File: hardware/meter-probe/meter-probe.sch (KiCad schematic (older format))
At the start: 0 parts

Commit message: Added some sheets and more components to the main board schematics
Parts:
- added C? (x2): 1uF, symbol Device:C
- added C?: 22nF, symbol Device:C
- added C?: 0.1uF, symbol Device:C
- added J?: Conn_01x05, symbol Connector_Generic:Conn_01x05
- added SW?: SW_Key_6425_0101, lib_fp:SW_Key_6425_0101, symbol Marquadt_Switch:SW_Key_6425_0101
- added U?: RT9193, Package_TO_SOT_SMD:SOT-23-5, symbol Project:RT9193
- added U?: TCS3472, lib_fp:AMS_TCS3472_DFN-6, symbol Project:TCS3472
- added U?: P82B96, Package_SO:SOIC-8_3.9x4.9mm_P1.27mm, symbol Interface_Expansion:P82B96
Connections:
- new net: C?.1, U?.4 (BP)
- new net: U?.2 (RXD-SDA), U?.3 (TXD-SDA)
- new net: U?.5 (TXD-SCL), U?.6 (RXD-SCL)
- new net +3V3: C?.1, C?.2, U?.1 (VDD), U?.5 (VOUT)
- new net +5V: C?.1, U?.1 (VIN), U?.3 (EN), U?.8 (VCC)
- new net GND: C?.1, C?.2, C?.2, C?.2, U?.2 (GND), U?.3 (GND), U?.4 (GND)

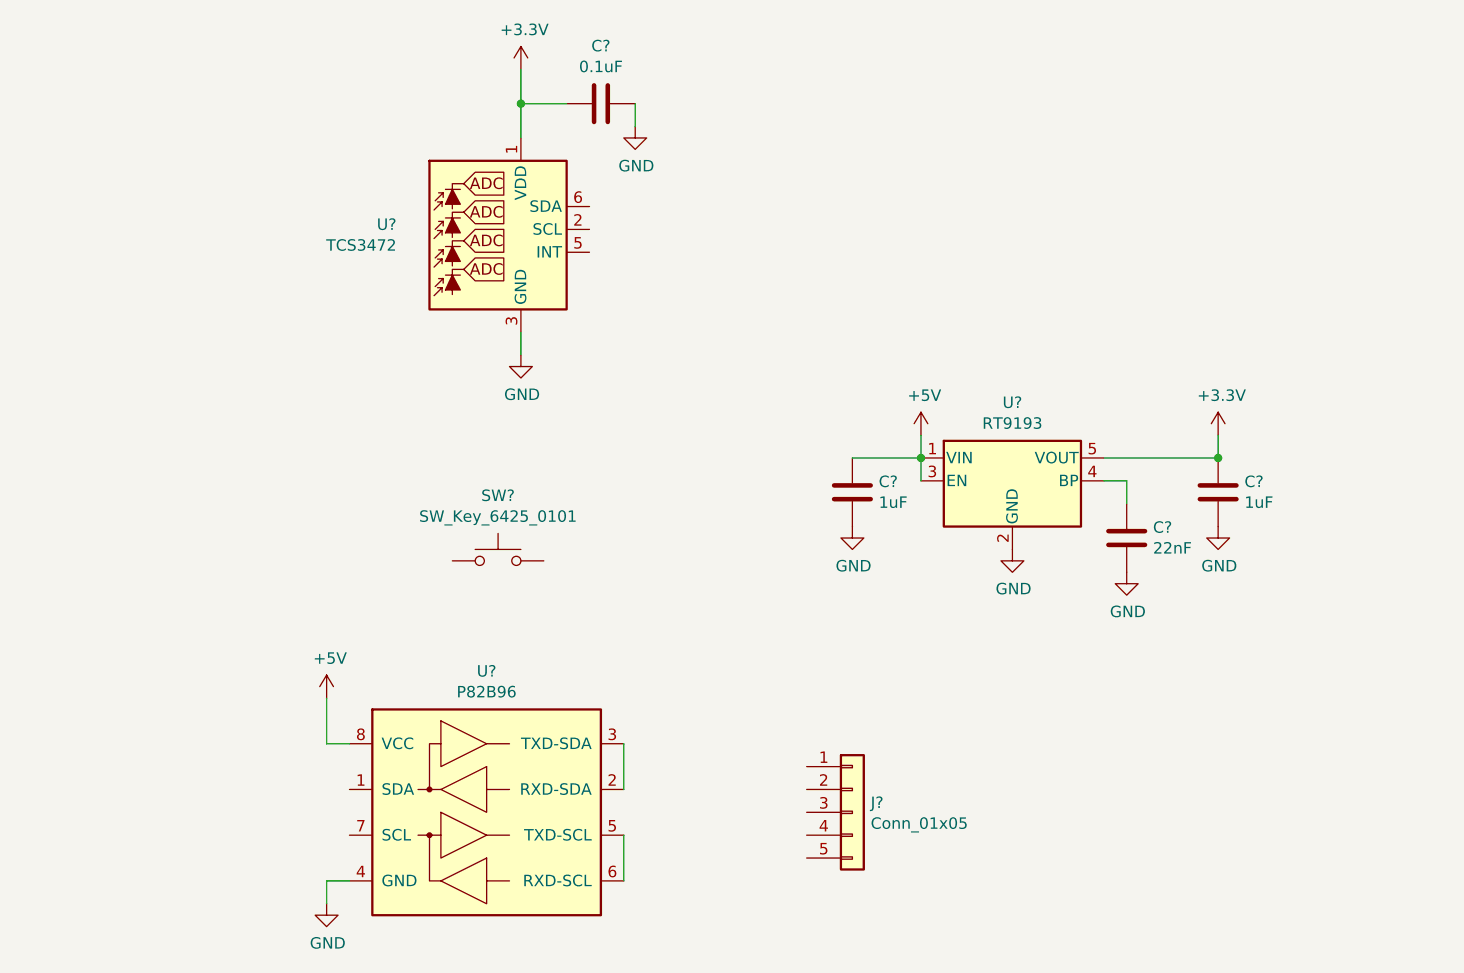
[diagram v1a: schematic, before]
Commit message: Added some off-board I2C interface elements
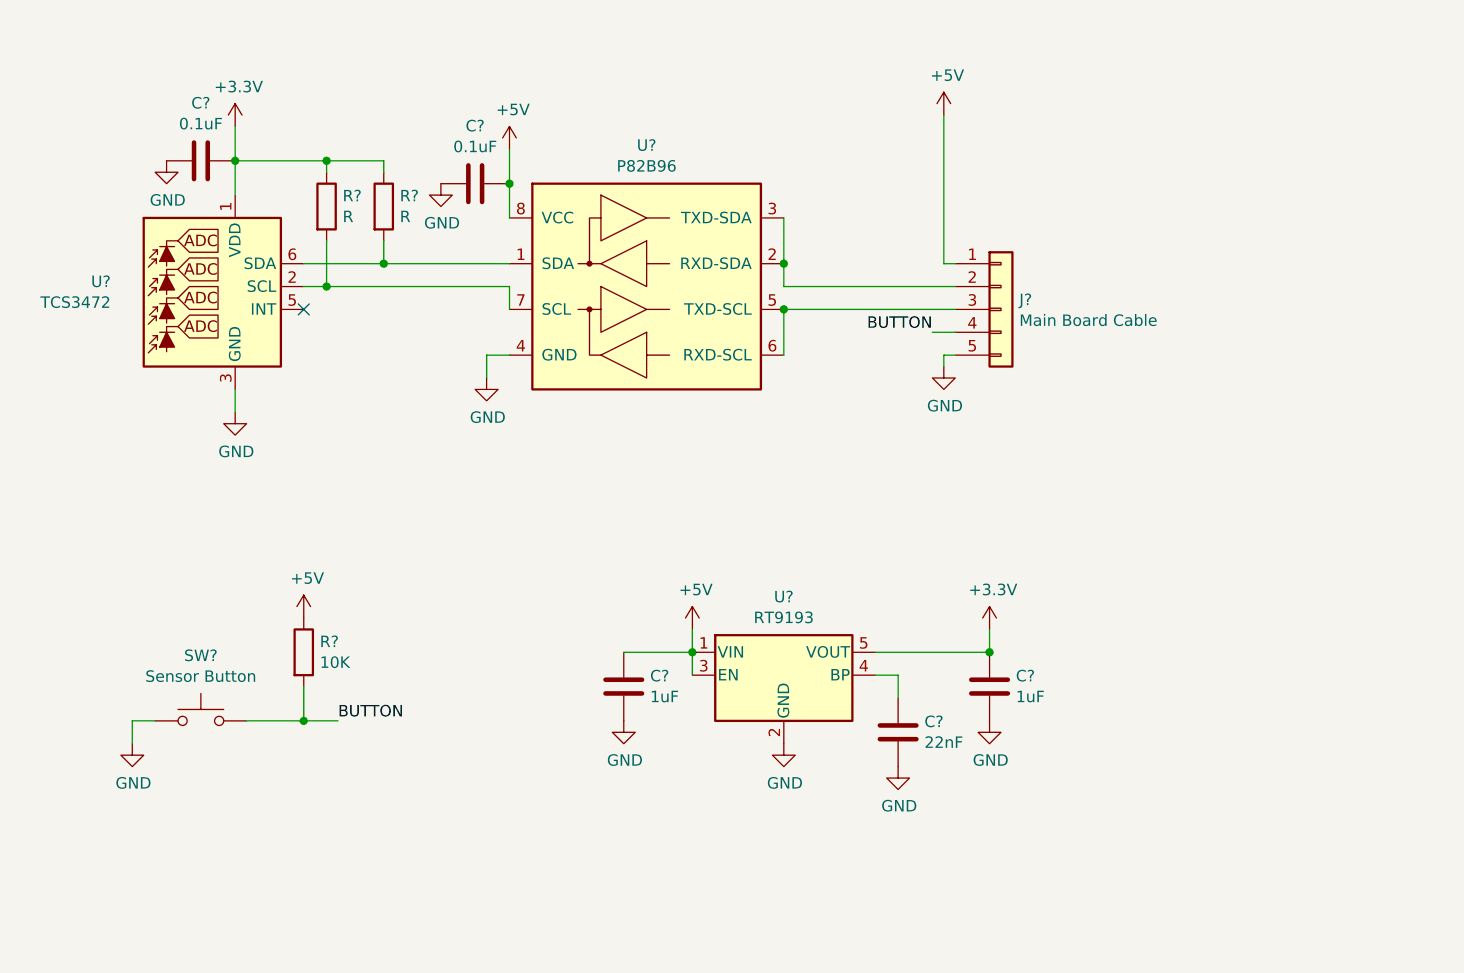
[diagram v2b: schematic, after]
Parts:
- added C?: 0.1uF, symbol Device:C
- added R? (x2): R, symbol Device:R
- added R?: 10K, symbol Device:R
- J?: value Conn_01x05 -> Main Board Cable
- SW?: value SW_Key_6425_0101 -> Sensor Button
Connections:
- net +3V3: now also C?.1, R?.1, R?.1; no longer C?.2
- net +5V: now also J?.1 (Pin_1), C?.1, R?.1
- net GND: now also C?.2, J?.5 (Pin_5), SW?.1, C?.2; no longer C?.1
- net at U?.2 (SCL): now also U?.7 (SCL), R?.2
- net at U?.6 (SDA): now also U?.1 (SDA), R?.2
- net BUTTON: now reaches SW?.2
- net BUTTON: now also J?.4 (Pin_4), R?.2
- net at U?.2 (RXD-SDA), U?.3 (TXD-SDA): now also J?.2 (Pin_2)
- net at U?.5 (TXD-SCL), U?.6 (RXD-SCL): now also J?.3 (Pin_3)
- no-connect marks 0 -> 1
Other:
- moved on the sheet: C?, J?, SW?, U?

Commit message: Sensor probe schematic and BOM associations complete
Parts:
- removed C? (x2): 1uF, symbol Device:C
- removed C?: 22nF, symbol Device:C
- removed C? (x2): 0.1uF, symbol Device:C
- removed R? (x2): R, symbol Device:R
- removed R?: 10K, symbol Device:R
- added C1, C2: 1uF, Capacitor_SMD:C_0805_2012Metric, symbol Device:C_Small
- added C3: 22nF, Capacitor_SMD:C_0805_2012Metric, symbol Device:C_Small
- added C4, C5: 0.1uF, Capacitor_SMD:C_0805_2012Metric, symbol Device:C_Small
- added Q1: BSS138, Package_TO_SOT_SMD:SOT-23, symbol Transistor_FET:BSS138
- added R1, R4, R5: 10K, Resistor_SMD:R_0805_2012Metric, symbol Device:R_Small
- added R2, R3: 2K, Resistor_SMD:R_0805_2012Metric, symbol Device:R_Small
- J1: renamed from J?; value Main Board Cable -> Main Board; footprint (none) -> Connector_Wire:SolderWire-1sqmm_1x06_P5.4mm_D1.4mm_OD2.7mm; symbol Connector_Generic:Conn_01x05 -> Connector_Generic:Conn_01x06
- SW1: renamed from SW?; Description (none) -> Switch 6425.0101 with button 827.100.011; Manufacturer (none) -> Marquardt Switches; Manufacturer PN (none) -> 6425.0101; Supplier (none) -> Mouser; Supplier PN (none) -> 979-6425.0101
- U1: renamed from U?; Description (none) -> IC REG LINEAR 3.3V 300MA SOT23-5; Manufacturer (none) -> Richtek USA Inc.; Manufacturer PN (none) -> RT9193-33GB; Supplier (none) -> Digi-Key; Supplier PN (none) -> 1028-1014-1-ND
- U2: renamed from U?; Description (none) -> IC COLOR CONV LIGHT-DGTL 6-DFN; Manufacturer (none) -> ams; Manufacturer PN (none) -> TCS34725FN; Supplier (none) -> Digi-Key; Supplier PN (none) -> TCS34725FNCT-ND
- U3: renamed from U?; Description (none) -> IC REDRIVER I2C 1CH 400KHZ 8SOIC; Manufacturer (none) -> Texas Instruments; Manufacturer PN (none) -> P82B96DR; Supplier (none) -> Digi-Key; Supplier PN (none) -> 296-20942-1-ND
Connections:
- net +3V3: now also C2.2, C4.1, Q1.1 (G), R2.1, R3.1, R4.1
- net +5V: now also J1.4 (Pin_4), C1.2, C5.1, R1.1, R5.1; no longer J1.1 (Pin_1)
- net GND: now also J1.3 (Pin_3), C1.1, C2.1, C3.1, C4.2, C5.2; no longer J1.5 (Pin_5)
- net at U1.4 (BP): now also C3.2
- net at U2.2 (SCL), U3.7 (SCL): now also R2.2
- net at U2.5 (INT): now also Q1.2 (S), R4.2
- net at U2.6 (SDA), U3.1 (SDA): now also R3.2
- net SDA: now reaches U3.2 (RXD-SDA), U3.3 (TXD-SDA)
- net SDA: now also J1.1 (Pin_1); no longer J1.2 (Pin_2)
- net SCL: now reaches U3.5 (TXD-SCL), U3.6 (RXD-SCL)
- net SCL: now also J1.5 (Pin_5); no longer J1.3 (Pin_3)
- net BUTTON renamed ~BUTTON
- net ~BUTTON: now also J1.6 (Pin_6), R1.2; no longer J1.4 (Pin_4)
- new net ~INT: J1.2 (Pin_2), Q1.3 (D), R5.2
- no-connect marks 1 -> 0
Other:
- note added: "Color light sensor"
- note added: "Level shifting"
- note added: "Main board cable connection"
- note added: "Note: All signals on the cable are at 5V,\nand are level-shifted on this board\nas necessary."
- note added: "Trigger button"
- note added: "Voltage regulator"
- moved on the sheet: SW1, U1, U3

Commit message: Updated wire connection footprint and PCB labeling
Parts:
- J1: footprint Connector_Wire:SolderWire-1sqmm_1x06_P5.4mm_D1.4mm_OD2.7mm -> Connector_Wire:SolderWire-0.1sqmm_1x06_P3.6mm_D0.4mm_OD1mm
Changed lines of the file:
@@
 F 0 "J1" H 5950 1850 50  0000 L CNN
 F 1 "Main Board" H 5900 1150 50  0000 L CNN
-F 2 "Connector_Wire:SolderWire-1sqmm_1x06_P5.4mm_D1.4mm_OD2.7mm" H 6000 1550 50  0001 C CNN
+F 2 "Connector_Wire:SolderWire-0.1sqmm_1x06_P3.6mm_D0.4mm_OD1mm" H 6000 1550 50  0001 C CNN
 F 3 "~" H 6000 1550 50  0001 C CNN
 	1    6000 1550

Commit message: Changed wire-to-board footprint for the meter probe
Created a footprint with more compact pin spacing, that includes
mechanical holes for attaching a cable tie that acts as a strain
relief for the cable.

Increased the length of the board, still within the package space,
to accommodate this change.
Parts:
- J1: footprint Connector_Wire:SolderWire-0.1sqmm_1x06_P3.6mm_D0.4mm_OD1mm -> lib_fp:SolderWire-0.1sqmm_1x06_Cable
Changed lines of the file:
@@
 F 0 "J1" H 5950 1850 50  0000 L CNN
 F 1 "Main Board" H 5900 1150 50  0000 L CNN
-F 2 "Connector_Wire:SolderWire-0.1sqmm_1x06_P3.6mm_D0.4mm_OD1mm" H 6000 1550 50  0001 C CNN
+F 2 "lib_fp:SolderWire-0.1sqmm_1x06_Cable" H 6000 1550 50  0001 C CNN
 F 3 "~" H 6000 1550 50  0001 C CNN
 	1    6000 1550

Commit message: Changed from 0805 to 0602 for passives, and fixed 22nF part
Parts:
- C1, C2: footprint Capacitor_SMD:C_0805_2012Metric -> Capacitor_SMD:C_0603_1608Metric; Description CAP CER 1UF 25V X7R 0805 -> CAP CER 1UF 25V X7R 0603; Manufacturer PN CL21B105KAFNNNE -> CL10B105KA8NNNC; Supplier PN 1276-1066-1-ND -> 1276-1184-1-ND
- C3: Description CAP CER 22PF 50V C0G/NP0 0805 -> CAP CER 0.022UF 50V C0G 0805; Manufacturer Samsung Electro-Mechanics -> TDK Corporation; Manufacturer PN CL21C220JBANNNC -> C2012C0G1H223J125AA; Supplier PN 1276-1047-1-ND -> 445-7522-1-ND
- C4, C5: footprint Capacitor_SMD:C_0805_2012Metric -> Capacitor_SMD:C_0603_1608Metric; Description CAP CER 0.1UF 25V X7R 0805 -> CAP CER 0.1UF 25V X7R 0603; Manufacturer PN CL21B104KACNNNC -> CL10B104KA8NNNC; Supplier PN 1276-1099-1-ND -> 1276-1006-1-ND
- J1: Description (none) -> WIRE-TO-BOARD
- R1, R4, R5: footprint Resistor_SMD:R_0805_2012Metric -> Resistor_SMD:R_0603_1608Metric; Description RES SMD 10K OHM 5% 1/8W 0805 -> RES SMD 10K OHM 5% 1/10W 0603; Manufacturer PN CRCW080510K0JNEA -> CRCW060310K0JNEA; Supplier PN 541-10KACT-ND -> 541-10KGCT-ND
- R2, R3: footprint Resistor_SMD:R_0805_2012Metric -> Resistor_SMD:R_0603_1608Metric; Description RES SMD 2K OHM 5% 1/8W 0805 -> RES SMD 2K OHM 5% 1/10W 0603; Manufacturer PN CRCW08052K00JNEA -> CRCW06032K00JNEA; Supplier PN 541-2.0KACT-ND -> 541-2.0KGCT-ND
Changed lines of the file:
@@
 F 2 "lib_fp:SolderWire-0.1sqmm_1x06_Cable" H 6000 1550 50  0001 C CNN
 F 3 "~" H 6000 1550 50  0001 C CNN
+F 4 "WIRE-TO-BOARD" H 6000 1550 50  0001 C CNN "Description"
 	1    6000 1550
 	1    0    0    -1
@@
 F 0 "R4" H 3559 2946 50  0000 L CNN
 F 1 "10K" H 3559 2855 50  0000 L CNN
-F 2 "Resistor_SMD:R_0805_2012Metric" H 3500 2900 50  0001 C CNN
+F 2 "Resistor_SMD:R_0603_1608Metric" H 3500 2900 50  0001 C CNN
 F 3 "https://www.vishay.com/docs/20035/dcrcwe3.pdf" H 3500 2900 50  0001 C CNN
-F 4 "RES SMD 10K OHM 5% 1/8W 0805" H 3500 2900 50  0001 C CNN "Description"
+F 4 "RES SMD 10K OHM 5% 1/10W 0603" H 3500 2900 50  0001 C CNN "Description"
 F 5 "Vishay Dale" H 3500 2900 50  0001 C CNN "Manufacturer"
-F 6 "CRCW080510K0JNEA" H 3500 2900 50  0001 C CNN "Manufacturer PN"
+F 6 "CRCW060310K0JNEA" H 3500 2900 50  0001 C CNN "Manufacturer PN"
 F 7 "Digi-Key" H 3500 2900 50  0001 C CNN "Supplier"
-F 8 "541-10KACT-ND" H 3500 2900 50  0001 C CNN "Supplier PN"
+F 8 "541-10KGCT-ND" H 3500 2900 50  0001 C CNN "Supplier PN"
 	1    3500 2900
 	1    0    0    -1
@@
 F 0 "R5" H 4259 2946 50  0000 L CNN
 F 1 "10K" H 4259 2855 50  0000 L CNN
-F 2 "Resistor_SMD:R_0805_2012Metric" H 4200 2900 50  0001 C CNN
+F 2 "Resistor_SMD:R_0603_1608Metric" H 4200 2900 50  0001 C CNN
 F 3 "https://www.vishay.com/docs/20035/dcrcwe3.pdf" H 4200 2900 50  0001 C CNN
-F 4 "RES SMD 10K OHM 5% 1/8W 0805" H 4200 2900 50  0001 C CNN "Description"
+F 4 "RES SMD 10K OHM 5% 1/10W 0603" H 4200 2900 50  0001 C CNN "Description"
 F 5 "Vishay Dale" H 4200 2900 50  0001 C CNN "Manufacturer"
-F 6 "CRCW080510K0JNEA" H 4200 2900 50  0001 C CNN "Manufacturer PN"
+F 6 "CRCW060310K0JNEA" H 4200 2900 50  0001 C CNN "Manufacturer PN"
 F 7 "Digi-Key" H 4200 2900 50  0001 C CNN "Supplier"
-F 8 "541-10KACT-ND" H 4200 2900 50  0001 C CNN "Supplier PN"
+F 8 "541-10KGCT-ND" H 4200 2900 50  0001 C CNN "Supplier PN"
 	1    4200 2900
 	1    0    0    -1
@@
 F 0 "R2" H 2259 1646 50  0000 L CNN
 F 1 "2K" H 2259 1555 50  0000 L CNN
-F 2 "Resistor_SMD:R_0805_2012Metric" H 2200 1600 50  0001 C CNN
+F 2 "Resistor_SMD:R_0603_1608Metric" H 2200 1600 50  0001 C CNN
 F 3 "https://www.vishay.com/docs/20035/dcrcwe3.pdf" H 2200 1600 50  0001 C CNN
-F 4 "RES SMD 2K OHM 5% 1/8W 0805" H 2200 1600 50  0001 C CNN "Description"
+F 4 "RES SMD 2K OHM 5% 1/10W 0603" H 2200 1600 50  0001 C CNN "Description"
 F 5 "Vishay Dale" H 2200 1600 50  0001 C CNN "Manufacturer"
-F 6 "CRCW08052K00JNEA" H 2200 1600 50  0001 C CNN "Manufacturer PN"
+F 6 "CRCW06032K00JNEA" H 2200 1600 50  0001 C CNN "Manufacturer PN"
 F 7 "Digi-Key" H 2200 1600 50  0001 C CNN "Supplier"
-F 8 "541-2.0KACT-ND" H 2200 1600 50  0001 C CNN "Supplier PN"
+F 8 "541-2.0KGCT-ND" H 2200 1600 50  0001 C CNN "Supplier PN"
 	1    2200 1600
 	1    0    0    -1
@@
 F 0 "R3" H 2509 1646 50  0000 L CNN
 F 1 "2K" H 2509 1555 50  0000 L CNN
-F 2 "Resistor_SMD:R_0805_2012Metric" H 2450 1600 50  0001 C CNN
+F 2 "Resistor_SMD:R_0603_1608Metric" H 2450 1600 50  0001 C CNN
 F 3 "https://www.vishay.com/docs/20035/dcrcwe3.pdf" H 2450 1600 50  0001 C CNN
-F 4 "RES SMD 2K OHM 5% 1/8W 0805" H 2450 1600 50  0001 C CNN "Description"
+F 4 "RES SMD 2K OHM 5% 1/10W 0603" H 2450 1600 50  0001 C CNN "Description"
 F 5 "Vishay Dale" H 2450 1600 50  0001 C CNN "Manufacturer"
-F 6 "CRCW08052K00JNEA" H 2450 1600 50  0001 C CNN "Manufacturer PN"
+F 6 "CRCW06032K00JNEA" H 2450 1600 50  0001 C CNN "Manufacturer PN"
 F 7 "Digi-Key" H 2450 1600 50  0001 C CNN "Supplier"
-F 8 "541-2.0KACT-ND" H 2450 1600 50  0001 C CNN "Supplier PN"
+F 8 "541-2.0KGCT-ND" H 2450 1600 50  0001 C CNN "Supplier PN"
 	1    2450 1600
 	1    0    0    -1
@@
 F 0 "C4" V 1371 1400 50  0000 C CNN
 F 1 "0.1uF" V 1462 1400 50  0000 C CNN
-F 2 "Capacitor_SMD:C_0805_2012Metric" H 1600 1400 50  0001 C CNN
-F 3 "https://media.digikey.com/pdf/Data%20Sheets/Samsung%20PDFs/CL21B104KACNNNC_Spec.pdf" H 1600 1400 50  0001 C CNN
-F 4 "CAP CER 0.1UF 25V X7R 0805" H 1600 1400 50  0001 C CNN "Description"
+F 2 "Capacitor_SMD:C_0603_1608Metric" H 1600 1400 50  0001 C CNN
+F 3 "https://media.digikey.com/pdf/Data%20Sheets/Samsung%20PDFs/CL_Series_MLCC_ds.pdf" H 1600 1400 50  0001 C CNN
+F 4 "CAP CER 0.1UF 25V X7R 0603" H 1600 1400 50  0001 C CNN "Description"
 F 5 "Samsung Electro-Mechanics" H 1600 1400 50  0001 C CNN "Manufacturer"
-F 6 "CL21B104KACNNNC" H 1600 1400 50  0001 C CNN "Manufacturer PN"
+F 6 "CL10B104KA8NNNC" H 1600 1400 50  0001 C CNN "Manufacturer PN"
 F 7 "Digi-Key" H 1600 1400 50  0001 C CNN "Supplier"
-F 8 "1276-1099-1-ND" H 1600 1400 50  0001 C CNN "Supplier PN"
+F 8 "1276-1006-1-ND" H 1600 1400 50  0001 C CNN "Supplier PN"
 	1    1600 1400
 	0    1    1    0
@@
 F 0 "C5" V 2871 1500 50  0000 C CNN
 F 1 "0.1uF" V 2962 1500 50  0000 C CNN
-F 2 "Capacitor_SMD:C_0805_2012Metric" H 3100 1500 50  0001 C CNN
-F 3 "https://media.digikey.com/pdf/Data%20Sheets/Samsung%20PDFs/CL21B104KACNNNC_Spec.pdf" H 3100 1500 50  0001 C CNN
-F 4 "CAP CER 0.1UF 25V X7R 0805" H 3100 1500 50  0001 C CNN "Description"
+F 2 "Capacitor_SMD:C_0603_1608Metric" H 3100 1500 50  0001 C CNN
+F 3 "https://media.digikey.com/pdf/Data%20Sheets/Samsung%20PDFs/CL_Series_MLCC_ds.pdf" H 3100 1500 50  0001 C CNN
+F 4 "CAP CER 0.1UF 25V X7R 0603" H 3100 1500 50  0001 C CNN "Description"
 F 5 "Samsung Electro-Mechanics" H 3100 1500 50  0001 C CNN "Manufacturer"
-F 6 "CL21B104KACNNNC" H 3100 1500 50  0001 C CNN "Manufacturer PN"
+F 6 "CL10B104KA8NNNC" H 3100 1500 50  0001 C CNN "Manufacturer PN"
 F 7 "Digi-Key" H 3100 1500 50  0001 C CNN "Supplier"
-F 8 "1276-1099-1-ND" H 3100 1500 50  0001 C CNN "Supplier PN"
+F 8 "1276-1006-1-ND" H 3100 1500 50  0001 C CNN "Supplier PN"
 	1    3100 1500
 	0    1    1    0
@@
 F 0 "R1" H 1759 4096 50  0000 L CNN
 F 1 "10K" H 1759 4005 50  0000 L CNN
-F 2 "Resistor_SMD:R_0805_2012Metric" H 1700 4050 50  0001 C CNN
+F 2 "Resistor_SMD:R_0603_1608Metric" H 1700 4050 50  0001 C CNN
 F 3 "https://www.vishay.com/docs/20035/dcrcwe3.pdf" H 1700 4050 50  0001 C CNN
-F 4 "RES SMD 10K OHM 5% 1/8W 0805" H 1700 4050 50  0001 C CNN "Description"
+F 4 "RES SMD 10K OHM 5% 1/10W 0603" H 1700 4050 50  0001 C CNN "Description"
 F 5 "Vishay Dale" H 1700 4050 50  0001 C CNN "Manufacturer"
-F 6 "CRCW080510K0JNEA" H 1700 4050 50  0001 C CNN "Manufacturer PN"
+F 6 "CRCW060310K0JNEA" H 1700 4050 50  0001 C CNN "Manufacturer PN"
 F 7 "Digi-Key" H 1700 4050 50  0001 C CNN "Supplier"
-F 8 "541-10KACT-ND" H 1700 4050 50  0001 C CNN "Supplier PN"
+F 8 "541-10KGCT-ND" H 1700 4050 50  0001 C CNN "Supplier PN"
 	1    1700 4050
 	1    0    0    -1
@@
 F 0 "C1" H 2908 4154 50  0000 R CNN
 F 1 "1uF" H 2908 4245 50  0000 R CNN
-F 2 "Capacitor_SMD:C_0805_2012Metric" H 3000 4200 50  0001 C CNN
-F 3 "http://www.samsungsem.com/kr/support/product-search/mlcc/__icsFiles/afieldfile/2019/03/18/Data%20sheet_CL21B105KAFNNNE.pdf" H 3000 4200 50  0001 C CNN
-F 4 "CAP CER 1UF 25V X7R 0805" H 3000 4200 50  0001 C CNN "Description"
+F 2 "Capacitor_SMD:C_0603_1608Metric" H 3000 4200 50  0001 C CNN
+F 3 "https://media.digikey.com/pdf/Data%20Sheets/Samsung%20PDFs/CL10B105KA8NNNC_char.pdf" H 3000 4200 50  0001 C CNN
+F 4 "CAP CER 1UF 25V X7R 0603" H 3000 4200 50  0001 C CNN "Description"
 F 5 "Samsung Electro-Mechanics" H 3000 4200 50  0001 C CNN "Manufacturer"
-F 6 "CL21B105KAFNNNE" H 3000 4200 50  0001 C CNN "Manufacturer PN"
+F 6 "CL10B105KA8NNNC" H 3000 4200 50  0001 C CNN "Manufacturer PN"
 F 7 "Digi-Key" H 3000 4200 50  0001 C CNN "Supplier"
-F 8 "1276-1066-1-ND" H 3000 4200 50  0001 C CNN "Supplier PN"
+F 8 "1276-1184-1-ND" H 3000 4200 50  0001 C CNN "Supplier PN"
 	1    3000 4200
 	-1   0    0    1
@@
 F 0 "C2" H 4508 4154 50  0000 R CNN
 F 1 "1uF" H 4508 4245 50  0000 R CNN
-F 2 "Capacitor_SMD:C_0805_2012Metric" H 4600 4200 50  0001 C CNN
-F 3 "http://www.samsungsem.com/kr/support/product-search/mlcc/__icsFiles/afieldfile/2019/03/18/Data%20sheet_CL21B105KAFNNNE.pdf" H 4600 4200 50  0001 C CNN
-F 4 "CAP CER 1UF 25V X7R 0805" H 4600 4200 50  0001 C CNN "Description"
+F 2 "Capacitor_SMD:C_0603_1608Metric" H 4600 4200 50  0001 C CNN
+F 3 "https://media.digikey.com/pdf/Data%20Sheets/Samsung%20PDFs/CL10B105KA8NNNC_char.pdf" H 4600 4200 50  0001 C CNN
+F 4 "CAP CER 1UF 25V X7R 0603" H 4600 4200 50  0001 C CNN "Description"
 F 5 "Samsung Electro-Mechanics" H 4600 4200 50  0001 C CNN "Manufacturer"
-F 6 "CL21B105KAFNNNE" H 4600 4200 50  0001 C CNN "Manufacturer PN"
+F 6 "CL10B105KA8NNNC" H 4600 4200 50  0001 C CNN "Manufacturer PN"
 F 7 "Digi-Key" H 4600 4200 50  0001 C CNN "Supplier"
-F 8 "1276-1066-1-ND" H 4600 4200 50  0001 C CNN "Supplier PN"
+F 8 "1276-1184-1-ND" H 4600 4200 50  0001 C CNN "Supplier PN"
 	1    4600 4200
 	-1   0    0    1
@@
 F 1 "22nF" H 4108 4445 50  0000 R CNN
 F 2 "Capacitor_SMD:C_0805_2012Metric" H 4200 4400 50  0001 C CNN
-F 3 "http://www.samsungsem.com/kr/support/product-search/mlcc/__icsFiles/afieldfile/2017/03/07/Data%20sheet_CL21C220JBANNNC.pdf" H 4200 4400 50  0001 C CNN
-F 4 "CAP CER 22PF 50V C0G/NP0 0805" H 4200 4400 50  0001 C CNN "Description"
-F 5 "Samsung Electro-Mechanics" H 4200 4400 50  0001 C CNN "Manufacturer"
-F 6 "CL21C220JBANNNC" H 4200 4400 50  0001 C CNN "Manufacturer PN"
+F 3 "https://product.tdk.com/info/en/documents/chara_sheet/C2012C0G1H223J125AA.pdf" H 4200 4400 50  0001 C CNN
+F 4 "CAP CER 0.022UF 50V C0G 0805" H 4200 4400 50  0001 C CNN "Description"
+F 5 "TDK Corporation" H 4200 4400 50  0001 C CNN "Manufacturer"
+F 6 "C2012C0G1H223J125AA" H 4200 4400 50  0001 C CNN "Manufacturer PN"
 F 7 "Digi-Key" H 4200 4400 50  0001 C CNN "Supplier"
-F 8 "1276-1047-1-ND" H 4200 4400 50  0001 C CNN "Supplier PN"
+F 8 "445-7522-1-ND" H 4200 4400 50  0001 C CNN "Supplier PN"
 	1    4200 4400
 	-1   0    0    1
